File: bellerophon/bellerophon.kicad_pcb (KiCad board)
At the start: 2 copper layers, 55 x 100 mm, 27 parts, among them IC1 L7805ACV, IC2 Adafruit_MPL3115A2, Q1 IRLB8721PBF, Q2 IRLB8721PBF, U1 Adafruit_ICM20948, U2 Teensy4.0, U3 Adafruit SPI Flash SD Card

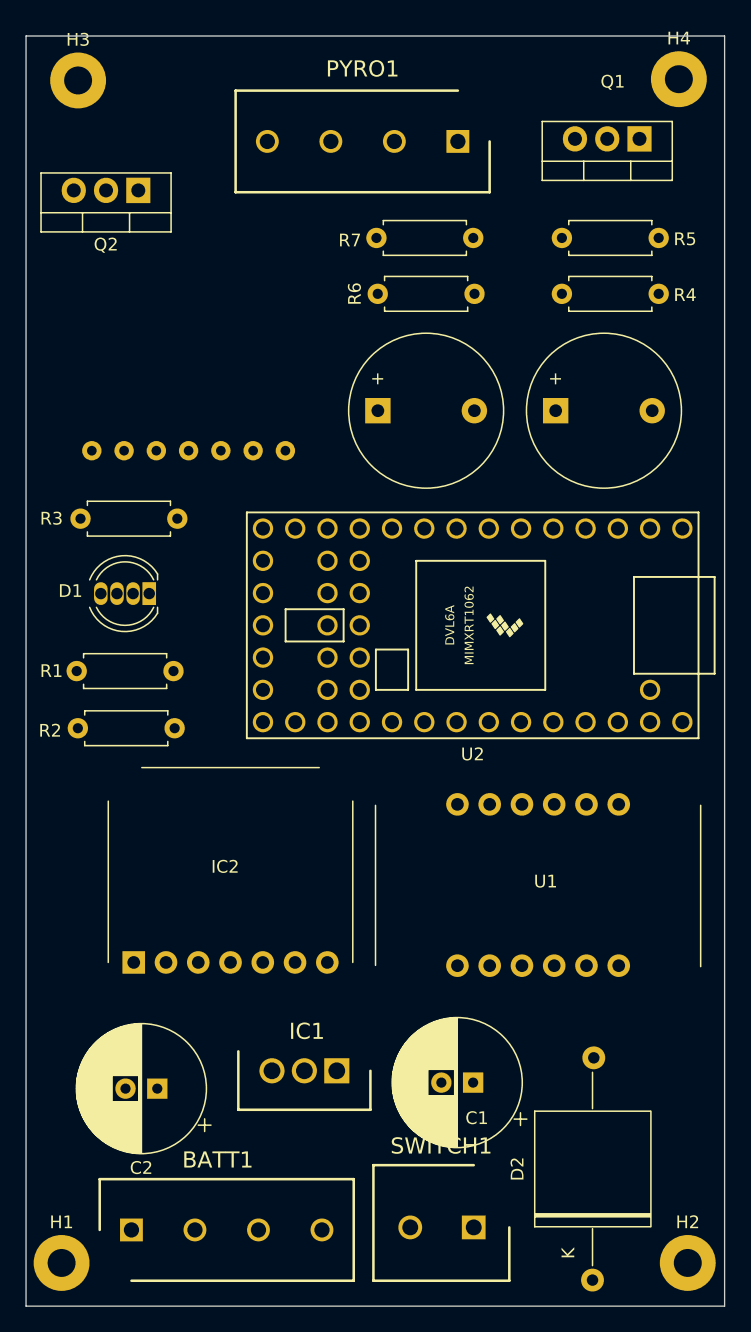
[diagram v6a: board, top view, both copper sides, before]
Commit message: curved board edges and reduced height to 98 mm
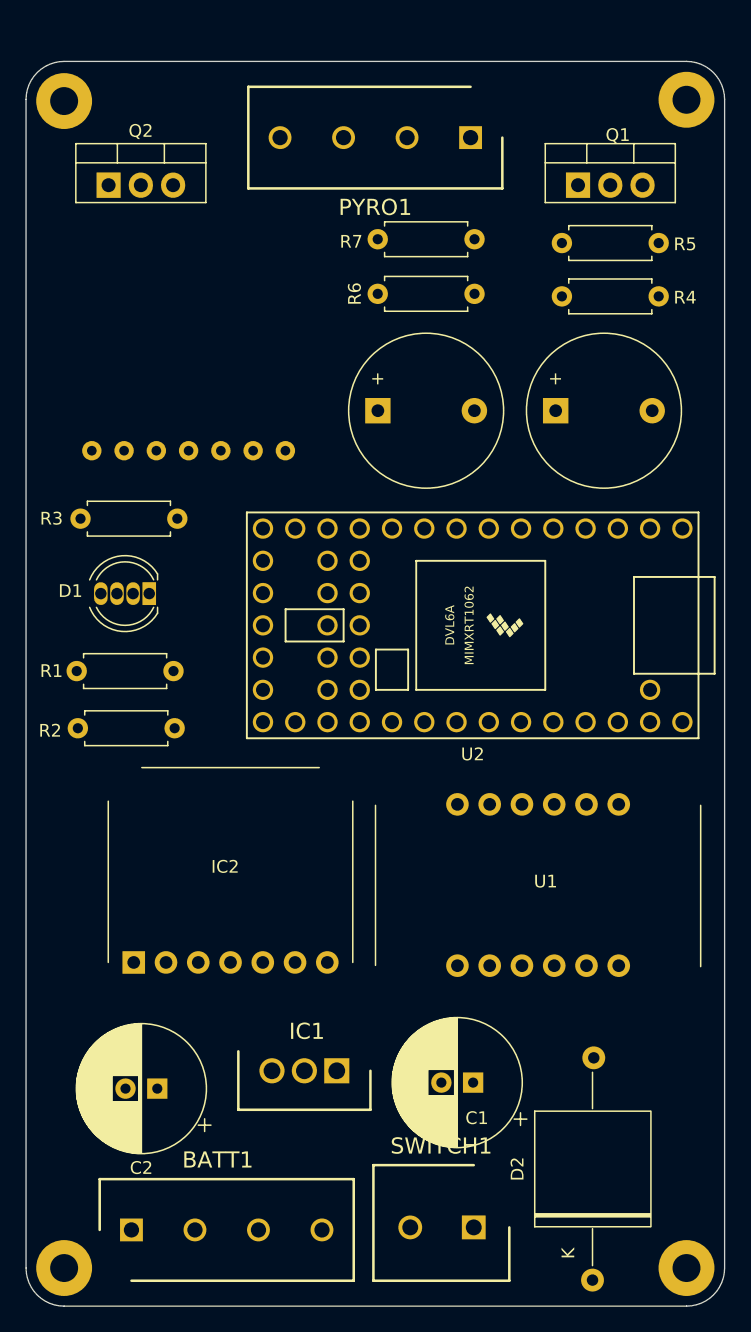
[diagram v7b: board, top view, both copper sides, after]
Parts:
- moved Q1 6.06 mm to (103.5, 71.7), turned to 0 degrees
- moved Q2 2.38 mm to (66.5, 71.7), turned to 0 degrees
- moved H3 1.96 mm to (63.0, 65.1)
- moved H4 1.73 mm to (112.0, 65.0)
- moved PYRO1 1.04 mm to (95.0, 68.0)
- moved H1 0.45 mm to (63.0, 157.0)
- moved H2 0.41 mm to (112.0, 157.0)
- moved R5 0.40 mm to (102.2, 76.3)
- moved R4 0.20 mm to (109.8, 80.5)
- moved R7 0.14 mm to (95.3, 76.0)
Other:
- board size 55 x 100 mm -> 55 x 98 mm
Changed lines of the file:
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@@
   (net 65 "BZR2")
   (footprint "Package_TO_SOT_THT:TO-220-3_Vertical" (layer "F.Cu")
-    (at 108.3 68.1 180)
+    (at 103.46 71.745)
     (descr "TO-220-3, Vertical, RM 2.54mm, see https://www.vishay.com/docs/66542/to-220-1.pdf")
     (tags "TO-220-3 Vertical RM 2.54mm")
@@
     (property "Sheetname" "")
     (attr through_hole)
-    (fp_text reference "Q1" (at 2.1 4.5) (layer "F.SilkS")
-      (effects (font (size 1 1) (thickness 0.15)))
-    )
-    (fp_text value "IRLB8721PBF" (at 2.54 2.5) (layer "F.Fab")
-      (effects (font (size 1 1) (thickness 0.15)))
-    )
-    (fp_text user "${REFERENCE}" (at 2.1 4.5) (layer "F.Fab")
+    (fp_text reference "Q1" (at 3.14 -3.945) (layer "F.SilkS")
+      (effects (font (size 1 1) (thickness 0.15)))
+    )
+    (fp_text value "IRLB8721PBF" (at 8.44 -0.9 90) (layer "F.Fab")
+      (effects (font (size 0.7 0.7) (thickness 0.1)))
+    )
+    (fp_text user "${REFERENCE}" (at -4.26 -1.245) (layer "F.Fab")
       (effects (font (size 1 1) (thickness 0.15)))
     )
@@
     (fp_line (start 0.69 -3.15) (end 0.69 -1.88) (layer "F.Fab") (width 0.1))
     (fp_line (start -2.46 1.25) (end 7.54 1.25) (layer "F.Fab") (width 0.1))
-    (pad "1" thru_hole rect (at 0 0 180) (size 1.905 2) (drill 1.1) (layers *.Cu *.Mask)
+    (pad "1" thru_hole rect (at 0 0) (size 1.905 2) (drill 1.1) (layers *.Cu *.Mask)
       (net 12 "Net-(Q1-Pad1)") (pinfunction "G") (pintype "input"))
-    (pad "2" thru_hole oval (at 2.54 0 180) (size 1.905 2) (drill 1.1) (layers *.Cu *.Mask)
+    (pad "2" thru_hole oval (at 2.54 0) (size 1.905 2) (drill 1.1) (layers *.Cu *.Mask)
       (net 62 "Net-(PYRO1-Pad1)") (pinfunction "D") (pintype "passive"))
-    (pad "3" thru_hole oval (at 5.08 0 180) (size 1.905 2) (drill 1.1) (layers *.Cu *.Mask)
+    (pad "3" thru_hole oval (at 5.08 0) (size 1.905 2) (drill 1.1) (layers *.Cu *.Mask)
       (net 1 "GND") (pinfunction "S") (pintype "passive"))
     (model "${KICAD6_3DMODEL_DIR}/Package_TO_SOT_THT.3dshapes/TO-220-3_Vertical.wrl"
@@
   )
   (footprint "MountingHole:MountingHole_2.2mm_M2_Pad" (layer "F.Cu")
-    (at 62.8 156.6)
+    (at 63 157)
     (descr "Mounting Hole 2.2mm, M2")
     (tags "mounting hole 2.2mm m2")
@@
     (property "Sheetname" "")
     (attr exclude_from_pos_files)
-    (fp_text reference "H1" (at 0 -3.2) (layer "F.SilkS")
-      (effects (font (size 1 1) (thickness 0.15)))
-    )
-    (fp_text value "MountingHole_Pad" (at 0 3.2) (layer "F.Fab")
+    (fp_text reference "H1" (at 0 -3.2) (layer "F.SilkS") hide
+      (effects (font (size 1 1) (thickness 0.15)))
+    )
+    (fp_text value "MountingHole_Pad" (at 0 3.2) (layer "F.Fab") hide
       (effects (font (size 1 1) (thickness 0.15)))
     )
@@
   )
   (footprint "Resistor_THT:R_Axial_DIN0207_L6.3mm_D2.5mm_P7.62mm_Horizontal" (layer "F.Cu")
-    (at 95.21 75.9 180)
+    (at 95.31 76 180)
     (descr "Resistor, Axial_DIN0207 series, Axial, Horizontal, pin pitch=7.62mm, 0.25W = 1/4W, length*diameter=6.3*2.5mm^2, http://cdn-reichelt.de/documents/datenblatt/B400/1_4W%23YAG.pdf")
     (tags "Resistor Axial_DIN0207 series Axial Horizontal pin pitch 7.62mm 0.25W = 1/4W length 6.3mm diameter 2.5mm")
@@
       (effects (font (size 1 1) (thickness 0.15)))
     )
-    (fp_text value "470 ohms" (at -1.59 -0.1 270) (layer "F.Fab")
+    (fp_text value "470 ohms" (at -1.59 0.2 270) (layer "F.Fab")
       (effects (font (size 0.5 0.5) (thickness 0.125)))
     )
@@
   )
   (footprint "MountingHole:MountingHole_2.2mm_M2_Pad" (layer "F.Cu")
-    (at 111.4 63.4)
+    (at 112 65.02132)
     (descr "Mounting Hole 2.2mm, M2")
     (tags "mounting hole 2.2mm m2")
@@
     (property "Sheetname" "")
     (attr exclude_from_pos_files)
-    (fp_text reference "H4" (at 0 -3.2) (layer "F.SilkS")
-      (effects (font (size 1 1) (thickness 0.15)))
-    )
-    (fp_text value "MountingHole_Pad" (at -1.15 4.4) (layer "F.Fab")
+    (fp_text reference "H4" (at 0 -3.2) (layer "F.SilkS") hide
+      (effects (font (size 1 1) (thickness 0.15)))
+    )
+    (fp_text value "MountingHole_Pad" (at -1.15 4.4) (layer "F.Fab") hide
       (effects (font (size 1 1) (thickness 0.15)))
     )
@@
   )
   (footprint "RS-Components:SHDR4W100P0X500_1X4_2000X800X1000P" (layer "F.Cu")
-    (at 94 68.3 180)
+    (at 95 68 180)
     (descr "REFP1/AIN6")
     (tags "Connector")
@@
     (property "Sheetname" "")
     (attr through_hole)
-    (fp_text reference "PYRO1" (at 7.5 5.7) (layer "F.SilkS")
+    (fp_text reference "PYRO1" (at 7.5 -5.5) (layer "F.SilkS")
       (effects (font (size 1.27 1.27) (thickness 0.254)))
     )
@@
       (effects (font (size 1.27 1.27) (thickness 0.254)))
     )
-    (fp_text user "${REFERENCE}" (at 7.5 5.7) (layer "F.Fab")
+    (fp_text user "${REFERENCE}" (at 7.5 -5.5) (layer "F.Fab")
       (effects (font (size 1.27 1.27) (thickness 0.254)))
     )
@@
   )
   (footprint "MountingHole:MountingHole_2.2mm_M2_Pad" (layer "F.Cu")
-    (at 112.1 156.6)
+    (at 112 157)
     (descr "Mounting Hole 2.2mm, M2")
     (tags "mounting hole 2.2mm m2")
@@
     (property "Sheetname" "")
     (attr exclude_from_pos_files)
-    (fp_text reference "H2" (at 0 -3.2) (layer "F.SilkS")
-      (effects (font (size 1 1) (thickness 0.15)))
-    )
-    (fp_text value "MountingHole_Pad" (at 0 3.2) (layer "F.Fab")
+    (fp_text reference "H2" (at 0 -3.2) (layer "F.SilkS") hide
+      (effects (font (size 1 1) (thickness 0.15)))
+    )
+    (fp_text value "MountingHole_Pad" (at 3.5 6.3) (layer "F.Fab") hide
       (effects (font (size 1 1) (thickness 0.15)))
     )
@@
   )
   (footprint "MountingHole:MountingHole_2.2mm_M2_Pad" (layer "F.Cu")
-    (at 64.1 63.5)
+    (at 63 65.12132)
     (descr "Mounting Hole 2.2mm, M2")
     (tags "mounting hole 2.2mm m2")
@@
     (property "Sheetname" "")
     (attr exclude_from_pos_files)
-    (fp_text reference "H3" (at 0 -3.2) (layer "F.SilkS")
-      (effects (font (size 1 1) (thickness 0.15)))
-    )
-    (fp_text value "MountingHole_Pad" (at 0 3.2) (layer "F.Fab")
+    (fp_text reference "H3" (at 0 -3.2) (layer "F.SilkS") hide
+      (effects (font (size 1 1) (thickness 0.15)))
+    )
+    (fp_text value "MountingHole_Pad" (at 0 3.2) (layer "F.Fab") hide
       (effects (font (size 1 1) (thickness 0.15)))
     )
@@
       (effects (font (size 1 1) (thickness 0.15)))
     )
-    (fp_text user "${REFERENCE}" (at 0 -10.16 unlocked) (layer "F.Fab")
+    (fp_text user "${REFERENCE}" (at -0.1 -3.1 unlocked) (layer "F.Fab")
       (effects (font (size 1 1) (thickness 0.15)))
     )
@@
   )
   (footprint "Package_TO_SOT_THT:TO-220-3_Vertical" (layer "F.Cu")
-    (at 68.84 72.155 180)
+    (at 66.5 71.745)
     (descr "TO-220-3, Vertical, RM 2.54mm, see https://www.vishay.com/docs/66542/to-220-1.pdf")
     (tags "TO-220-3 Vertical RM 2.54mm")
@@
       (effects (font (size 1 1) (thickness 0.15)))
     )
-    (fp_text value "IRLB8721PBF" (at 2.54 2.5) (layer "F.Fab")
-      (effects (font (size 1 1) (thickness 0.15)))
+    (fp_text value "IRLB8721PBF" (at 8.44 -0.945 90) (layer "F.Fab")
+      (effects (font (size 0.7 0.7) (thickness 0.1)))
     )
     (fp_text user "${REFERENCE}" (at 2.54 -4.27) (layer "F.Fab")
@@
     (fp_line (start 0.69 -3.15) (end 0.69 -1.88) (layer "F.Fab") (width 0.1))
     (fp_line (start 7.54 -3.15) (end -2.46 -3.15) (layer "F.Fab") (width 0.1))
-    (pad "1" thru_hole rect (at 0 0 180) (size 1.905 2) (drill 1.1) (layers *.Cu *.Mask)
+    (pad "1" thru_hole rect (at 0 0) (size 1.905 2) (drill 1.1) (layers *.Cu *.Mask)
       (net 13 "Net-(Q2-Pad1)") (pinfunction "G") (pintype "input"))
-    (pad "2" thru_hole oval (at 2.54 0 180) (size 1.905 2) (drill 1.1) (layers *.Cu *.Mask)
+    (pad "2" thru_hole oval (at 2.54 0) (size 1.905 2) (drill 1.1) (layers *.Cu *.Mask)
       (net 63 "Net-(PYRO1-Pad4)") (pinfunction "D") (pintype "passive"))
-    (pad "3" thru_hole oval (at 5.08 0 180) (size 1.905 2) (drill 1.1) (layers *.Cu *.Mask)
+    (pad "3" thru_hole oval (at 5.08 0) (size 1.905 2) (drill 1.1) (layers *.Cu *.Mask)
       (net 1 "GND") (pinfunction "S") (pintype "passive"))
     (model "${KICAD6_3DMODEL_DIR}/Package_TO_SOT_THT.3dshapes/TO-220-3_Vertical.wrl"
@@
   )
   (footprint "Resistor_THT:R_Axial_DIN0207_L6.3mm_D2.5mm_P7.62mm_Horizontal" (layer "F.Cu")
-    (at 109.81 80.3 180)
+    (at 109.81 80.5 180)
     (descr "Resistor, Axial_DIN0207 series, Axial, Horizontal, pin pitch=7.62mm, 0.25W = 1/4W, length*diameter=6.3*2.5mm^2, http://cdn-reichelt.de/documents/datenblatt/B400/1_4W%23YAG.pdf")
     (tags "Resistor Axial_DIN0207 series Axial Horizontal pin pitch 7.62mm 0.25W = 1/4W length 6.3mm diameter 2.5mm")
@@
   )
   (footprint "Resistor_THT:R_Axial_DIN0207_L6.3mm_D2.5mm_P7.62mm_Horizontal" (layer "F.Cu")
-    (at 102.19 75.9)
+    (at 102.19 76.3)
     (descr "Resistor, Axial_DIN0207 series, Axial, Horizontal, pin pitch=7.62mm, 0.25W = 1/4W, length*diameter=6.3*2.5mm^2, http://cdn-reichelt.de/documents/datenblatt/B400/1_4W%23YAG.pdf")
     (tags "Resistor Axial_DIN0207 series Axial Horizontal pin pitch 7.62mm 0.25W = 1/4W length 6.3mm diameter 2.5mm")
@@
       (net 28 "unconnected-(U1-Pad12)") (pinfunction "CS") (pintype "bidirectional+no_connect") (solder_mask_margin 0.0508))
   )
-  (gr_rect (start 60 160) (end 115 60) (layer "Edge.Cuts") (width 0.1) (fill none))
+  (gr_line (start 63 160) (end 112 160) (layer "Edge.Cuts") (width 0.1))
+  (gr_arc (start 63 160) (mid 60.87868 159.12132) (end 60 157) (layer "Edge.Cuts") (width 0.1))
+  (gr_arc (start 60 65) (mid 60.87868 62.87868) (end 63 62) (layer "Edge.Cuts") (width 0.1))
+  (gr_arc (start 115 157) (mid 114.12132 159.12132) (end 112 160) (layer "Edge.Cuts") (width 0.1))
+  (gr_line (start 112 62) (end 63 62) (layer "Edge.Cuts") (width 0.1))
+  (gr_line (start 60 65) (end 60 157) (layer "Edge.Cuts") (width 0.1))
+  (gr_line (start 115 157) (end 115 65) (layer "Edge.Cuts") (width 0.1))
+  (gr_arc (start 112 62) (mid 114.12132 62.87868) (end 115 65) (layer "Edge.Cuts") (width 0.1))
 )
